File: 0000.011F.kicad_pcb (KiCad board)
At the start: 2 copper layers, 95 x 77 mm, 149 parts, among them J10 XH, J12 XH, J2 BH254, J3 BH254, J5 BH254, J6 NC3FAH1, J8 NC3FAH1, U11 TL072, U13 TL072, U14 TL072, U3 TL072, U4 TL072, U5 TL072, U7 TL072, U8 TL072

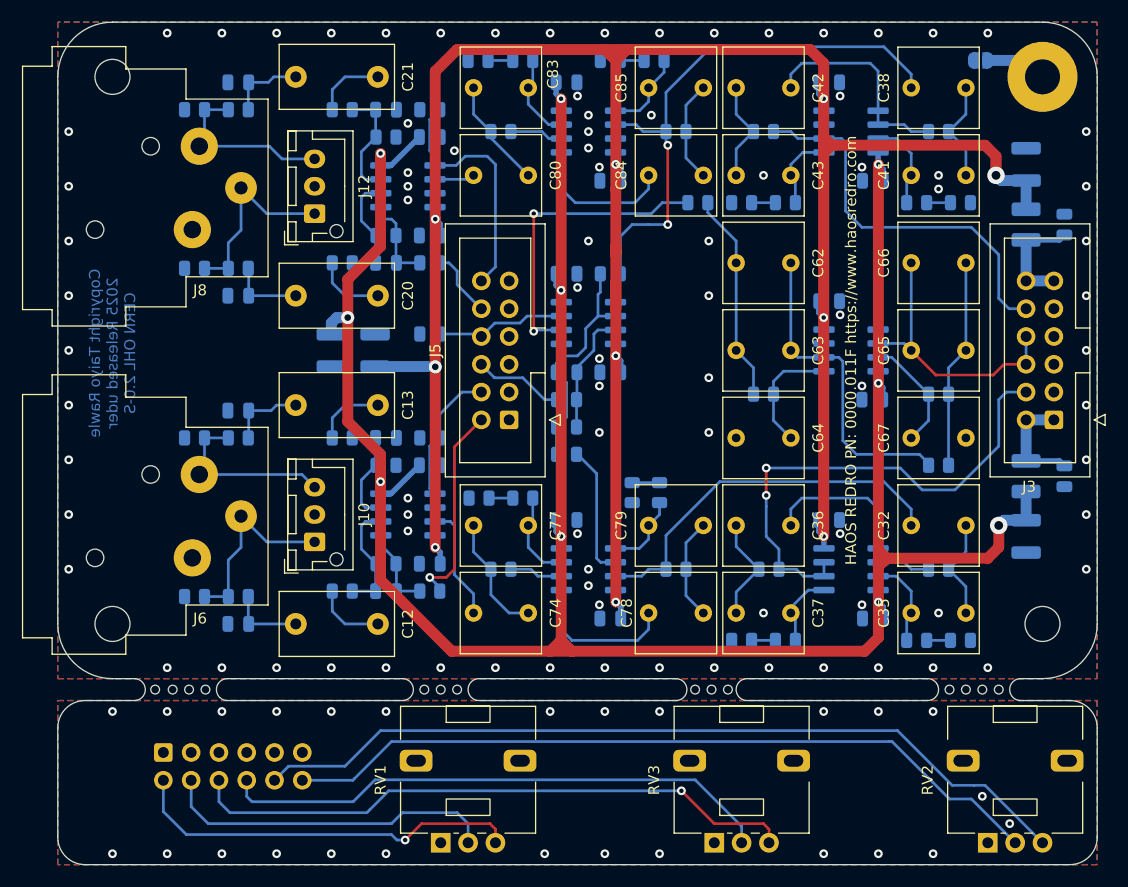
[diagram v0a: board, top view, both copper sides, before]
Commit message: Pot board made smaller using MicroMatch connectors. Snap-off holes tidied up, and gap increased to 2mm for compatibility with some PCB manufacturer's design rules.
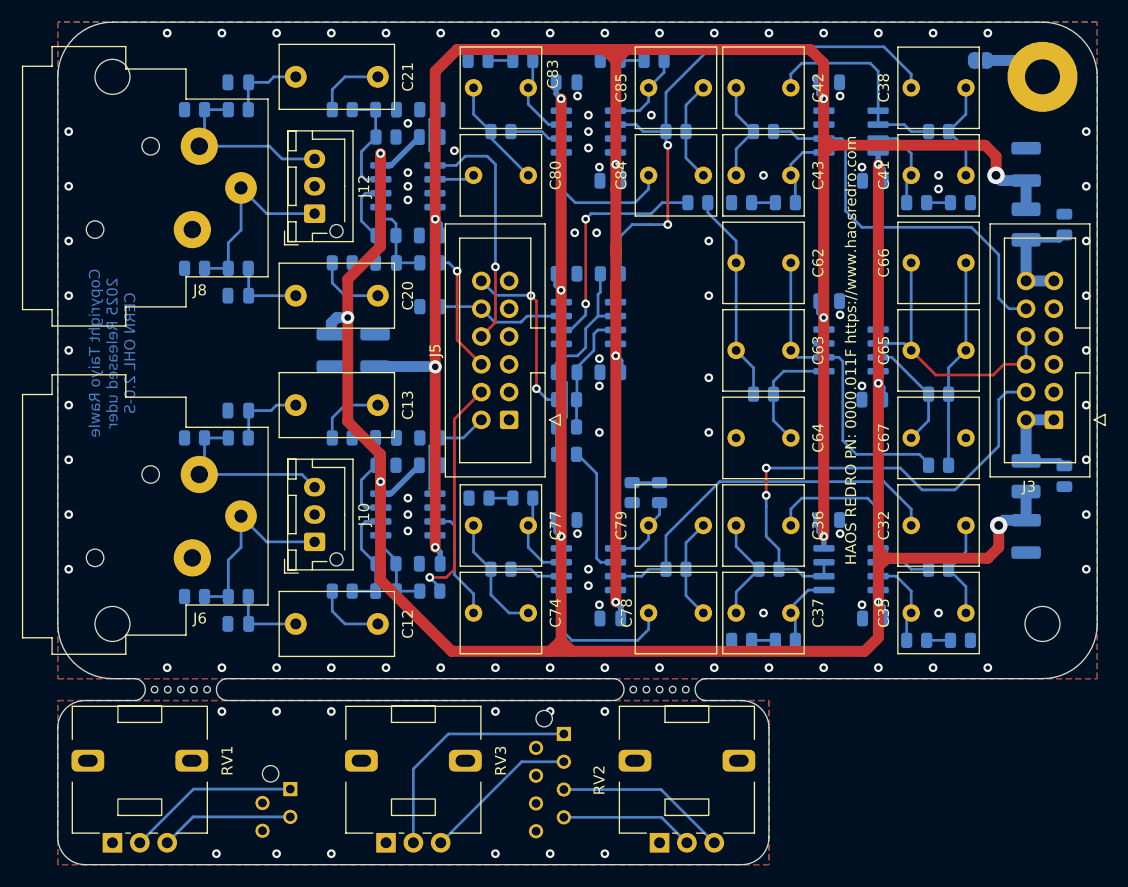
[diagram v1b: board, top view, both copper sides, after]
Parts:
- removed H10, H11, H12, H13, H14, H15, H16, H17, H18, H7, H8, H9: 0.8, HR_Parts:HOLE_0.8
- removed J2: BH254, Connector_IDC:IDC-Header_2x06_P2.54mm_Vertical
- added J1: MicroMatch, Connector_TE-Connectivity:TE_Micro-MaTch_215079-4_2x02_P1.27mm_Vertical, B.Cu at (76.3, 140.1)
- added J4: MicroMatch, Connector_TE-Connectivity:TE_Micro-MaTch_215079-8_2x04_P1.27mm_Vertical, B.Cu at (101.3, 135.1)
- H5, H6: value 0.8 -> snapline; footprint HR_Parts:HOLE_0.8 -> HR_Parts:SNAPOFF_5x0.6_P1.2
- moved H6 41.5 mm to (110.0, 131.0)
- moved RV1 30.0 mm to (60.0, 145.0)
- moved RV2 30.0 mm to (110.0, 145.0)
- moved RV3 30.0 mm to (85.0, 145.0)
- moved R5 2.50 mm to (89.0, 96.0)
- moved H5 2.35 mm to (66.2, 131.0)
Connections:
- J5 pad 10: /Input stage CH2/POTH -> /SPW
- J5 pad 12: /Input stage CH2/POTW -> /SPH
- J5 pad 2: /Input stage CH1/POTH -> /Input stage CH1/POTW
- J5 pad 4: /Input stage CH1/POTW -> /Input stage CH1/POTH
- J5 pad 6: /SPH -> /Input stage CH2/POTH
- J5 pad 8: /SPW -> /Input stage CH2/POTW
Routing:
- net Net-(J4-Pin_5): track 76.3 -> 15.8 mm
- net Net-(J4-Pin_7): track 70.4 -> 12.2 mm
- net Net-(J4-Pin_3): track 56.4 -> 14.3 mm, vias 1 -> 0
- net Net-(J4-Pin_1): track 51.0 -> 21.8 mm
- net Net-(J1-Pin_3): track 36.4 -> 12.2 mm, vias 1 -> 0
- net Net-(J1-Pin_1): track 30.9 -> 15.8 mm
- net /SPH: track 8.56 -> 16.1 mm, vias 0 -> 2
- net /Sub lowpass1/IN: track 29.1 -> 22.8 mm
- net /Input stage CH2/POTH: track 5.92 -> 11.3 mm, vias 0 -> 1
- net /Input stage CH2/POTW: track 23.0 -> 28.1 mm, vias 0 -> 1
- net /Input stage CH1/POTH: track 18.9 -> 21.4 mm
- net /Input stage CH1/POTW: track 12.6 -> 10.2 mm
- net Net-(J1-Pin_2): vias 26 -> 12
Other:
- outline, holes or cut-outs redrawn
